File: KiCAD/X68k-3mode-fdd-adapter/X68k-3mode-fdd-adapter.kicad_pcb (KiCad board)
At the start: 4 copper layers, 57.1 x 70 mm, 49 parts, among them J1 Conn_02x17_Odd_Even, J2 Double Row 3A Copper Alloy 34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, J3 Conn_01x04, J4 PH-4A, J5 SDIO, J6 Conn_01x04, J7 Conn_01x03_Pin, P1 USB_C_Plug_USB2.0, Q1 2SC2712, SW1 SW_DIP_x02, SW2 SW_SPDT, U1 CH32V003F4U6, U4 74HC153, U5 74HC153, U6 ULN2003A

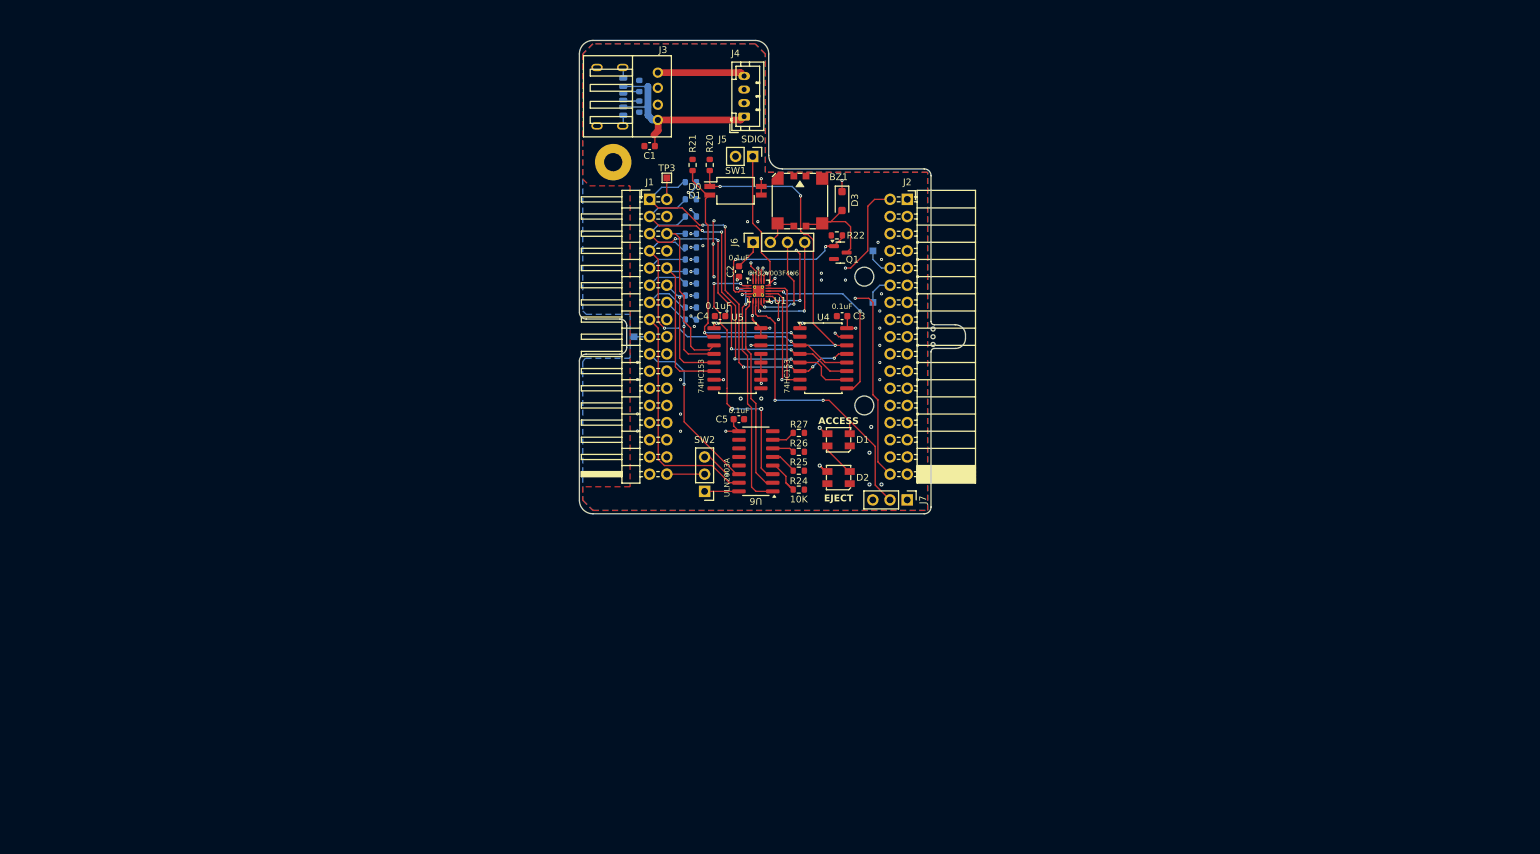
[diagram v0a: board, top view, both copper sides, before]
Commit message: フットプリントを一通り割り当てた
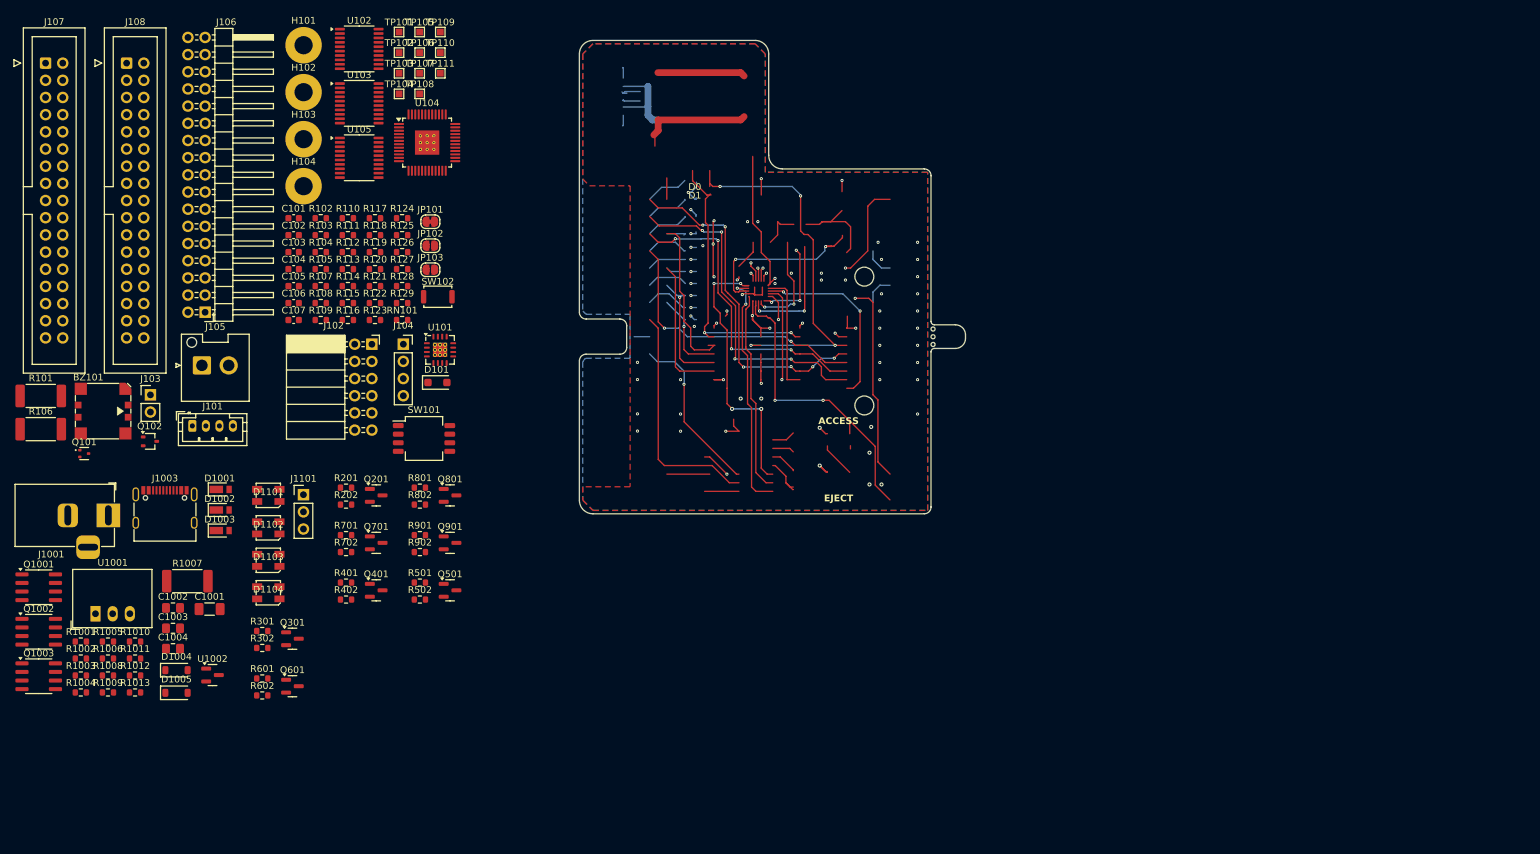
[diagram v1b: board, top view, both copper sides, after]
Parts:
- removed BZ1: Speaker, x68k-lib:UGCT7525AN4
- removed C1: 10uF, Capacitor_SMD:C_0603_1608Metric
- removed C2, C3, C4, C5: 0.1uF, Capacitor_SMD:C_0603_1608Metric
- removed D1, D2: SK6812MINI, x68k-lib:SK6812MINI-HS
- removed D3: SS2040FL, Diode_SMD:D_SOD-123F
- removed H1: MountingHole_Pad, MountingHole:MountingHole_2.7mm_M2.5_Pad
- removed J1: Conn_02x17_Odd_Even, x68k-lib:PinHeader_2x17_P2.54mm_Horizontal_Mirror
- removed J2: Double Row 3A Copper Alloy 34P Female Headers (PM254-2-17-W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, x68k-lib:PinSocket_2x17_P2.54mm_Horizontal_Mirror
- removed J3: Conn_01x04, x68k-lib:TE_AMP_171826-4
- removed J4: PH-4A, Connector_JST:JST_PH_B4B-PH-K_1x04_P2.00mm_Vertical
- removed J5: SDIO, Connector_PinHeader_2.54mm:PinHeader_1x02_P2.54mm_Vertical
- removed J6: Conn_01x04, Connector_PinSocket_2.54mm:PinSocket_1x04_P2.54mm_Vertical
- removed J7: Conn_01x03_Pin, Connector_PinHeader_2.54mm:PinHeader_1x03_P2.54mm_Vertical
- removed P1: USB_C_Plug_USB2.0, Connector_USB:USB_C_Receptacle_GCT_USB4125-xx-x-0190_6P_TopMnt_Horizontal
- removed Q1: 2SC2712, Package_TO_SOT_SMD:SOT-23
- removed R0, R1, R10, R11, R12, R13, R2, R3, R5, R6, R7: 1K, Resistor_SMD:R_0603_1608Metric
- removed R20, R21, R22, R24, R25, R26, R27: 10K, Resistor_SMD:R_0603_1608Metric
- removed R31, R32: 5.1k, Resistor_SMD:R_0603_1608Metric
- removed SW1: SW_DIP_x02, Button_Switch_SMD:SW_DIP_SPSTx02_Slide_Copal_CHS-02B_W7.62mm_P1.27mm
- removed SW2: SW_SPDT, Connector_PinHeader_2.54mm:PinHeader_1x03_P2.54mm_Vertical
- removed TP1, TP2, TP3, TP4: TestPoint, TestPoint:TestPoint_Pad_1.0x1.0mm
- removed U1: CH32V003F4U6, Package_DFN_QFN:QFN-20-1EP_3x3mm_P0.4mm_EP1.65x1.65mm_ThermalVias
- removed U4, U5: 74HC153, Package_SO:SO-16_5.3x10.2mm_P1.27mm
- removed U6: ULN2003A, Package_SO:SOP-16_3.9x9.9mm_P1.27mm
- added BZ101: Speaker, x68k-lib:UGCT7525AN4, F.Cu at (-8.43, 94.8)
- added C1001: 4.7uF 50V, Capacitor_SMD:C_1206_3216Metric_Pad1.33x1.80mm_HandSolder, F.Cu at (7.31, 124.1)
- added C1002: 22uF 25V, Capacitor_SMD:C_0805_2012Metric_Pad1.18x1.45mm_HandSolder, F.Cu at (1.90, 123.9)
- added C1003: 2.2uF 25V, Capacitor_SMD:C_0805_2012Metric_Pad1.18x1.45mm_HandSolder, F.Cu at (1.90, 126.9)
- added C1004: 2.2uF 25V, Capacitor_SMD:C_0805_2012Metric_Pad1.18x1.45mm_HandSolder, F.Cu at (1.90, 129.9)
- added C101: 0.1uF, Capacitor_SMD:C_0603_1608Metric, F.Cu at (19.7, 66.3)
- added C102: 0.1uF, Capacitor_SMD:C_0603_1608Metric, F.Cu at (19.7, 68.8)
- added C103: 0.1uF, Capacitor_SMD:C_0603_1608Metric, F.Cu at (19.7, 71.3)
- added C104: 0.1uF, Capacitor_SMD:C_0603_1608Metric, F.Cu at (19.7, 73.8)
- added C105: 0.1uF, Capacitor_SMD:C_0603_1608Metric, F.Cu at (19.7, 76.3)
- added C106: 0.1uF, Capacitor_SMD:C_0603_1608Metric, F.Cu at (19.7, 78.8)
- added C107: 0.1uF, Capacitor_SMD:C_0603_1608Metric, F.Cu at (19.7, 81.3)
- added D1001: CUHS20S30, x68k-lib:CUHS20S30 (US2H), F.Cu at (8.80, 106.4)
- added D1002: CUHS20S30, x68k-lib:CUHS20S30 (US2H), F.Cu at (8.80, 109.4)
- added D1003: CUHS20S30, x68k-lib:CUHS20S30 (US2H), F.Cu at (8.80, 112.5)
- added D1004: 1N60PW, Diode_SMD:D_SOD-123, F.Cu at (2.42, 133.1)
- added D1005: 1N60PW, Diode_SMD:D_SOD-123, F.Cu at (2.42, 136.5)
- added D101: SS2040FL, Diode_SMD:D_SOD-123F, F.Cu at (41.0, 90.6)
- added D1101: SK6812MINI, x68k-lib:SK6812MINI-HS, F.Cu at (16.0, 107.3)
- added D1102: SK6812MINI, x68k-lib:SK6812MINI-HS, F.Cu at (16.0, 112.1)
- added D1103: SK6812MINI, x68k-lib:SK6812MINI-HS, F.Cu at (16.0, 116.9)
- added D1104: SK6812MINI, x68k-lib:SK6812MINI-HS, F.Cu at (16.0, 121.7)
- added H101: MountingHole_Pad, MountingHole:MountingHole_2.7mm_M2.5_Pad, F.Cu at (21.2, 40.7)
- added H102: MountingHole_Pad, MountingHole:MountingHole_2.7mm_M2.5_Pad, F.Cu at (21.2, 47.7)
- added H103: MountingHole_Pad, MountingHole:MountingHole_2.7mm_M2.5_Pad, F.Cu at (21.2, 54.6)
- added H104: MountingHole_Pad, MountingHole:MountingHole_2.7mm_M2.5_Pad, F.Cu at (21.2, 61.6)
- added J1001: Barrel_Jack_Switch, Connector_BarrelJack:BarrelJack_Horizontal, F.Cu at (-7.66, 110.2)
- added J1003: USB_C_Receptacle_USB2.0_16P, Connector_USB:USB_C_Receptacle_G-Switch_GT-USB-7010ASV, F.Cu at (0.71, 110.3)
- added J101: 4pin, Connector_JST:JST_PH_B4B-PH-K_1x04_P2.00mm_Vertical, F.Cu at (4.76, 97.0)
- added J102: Conn_02x06_Odd_Even, Connector_PinSocket_2.54mm:PinSocket_2x06_P2.54mm_Horizontal, F.Cu at (31.3, 84.9)
- added J103: Conn_01x02, Connector_PinHeader_2.54mm:PinHeader_1x02_P2.54mm_Vertical, F.Cu at (-1.44, 92.4)
- added J104: Conn_01x04, Connector_PinSocket_2.54mm:PinSocket_1x04_P2.54mm_Vertical, F.Cu at (36.0, 84.9)
- added J105: Conn_01x02, Connector_JST:JST_VH_B2P-VH-FB-B_1x02_P3.96mm_Vertical, F.Cu at (6.18, 88.1)
- added J106: Conn_02x17_Odd_Even, x68k-lib:PinHeader_2x17_P2.54mm_Horizontal_Mirror, F.Cu at (4.11, 39.6)
- added J107: Conn_02x17_Odd_Even, Connector_IDC:IDC-Header_2x17_P2.54mm_Vertical, F.Cu at (-16.9, 43.4)
- added J108: Conn_02x17_Odd_Even, Connector_IDC:IDC-Header_2x17_P2.54mm_Vertical, F.Cu at (-4.96, 43.4)
- added J1101: Conn_01x03_Pin, Connector_PinHeader_2.54mm:PinHeader_1x03_P2.54mm_Vertical, F.Cu at (21.2, 107.2)
- added JP101: Jumper_2_Small_Bridged, Jumper:SolderJumper-2_P1.3mm_Bridged_RoundedPad1.0x1.5mm, F.Cu at (40.0, 66.8)
- added JP102: Jumper_2_Small_Open, Jumper:SolderJumper-2_P1.3mm_Open_RoundedPad1.0x1.5mm, F.Cu at (40.0, 70.4)
- added JP103: Jumper_2_Small_Open, Jumper:SolderJumper-2_P1.3mm_Open_RoundedPad1.0x1.5mm, F.Cu at (40.0, 73.9)
- added Q1001: FDS4935A, Package_SO:SOIC-8_3.9x4.9mm_P1.27mm, F.Cu at (-18.0, 120.9)
- added Q1002: FDS4935A, Package_SO:SOIC-8_3.9x4.9mm_P1.27mm, F.Cu at (-18.0, 127.4)
- added Q1003: FDS4935A, Package_SO:SOIC-8_3.9x4.9mm_P1.27mm, F.Cu at (-18.0, 134.0)
- added Q101: DTC143Z, Package_TO_SOT_SMD:SOT-523, F.Cu at (-11.2, 101.1)
- added Q102: 2SC2712, Package_TO_SOT_SMD:SOT-323_SC-70, F.Cu at (-1.51, 99.3)
- added Q201: BSS138, Package_TO_SOT_SMD:SOT-23, F.Cu at (32.0, 107.3)
- added Q301: BSS138, Package_TO_SOT_SMD:SOT-23, F.Cu at (19.6, 128.5)
- added Q401: BSS138, Package_TO_SOT_SMD:SOT-23, F.Cu at (32.0, 121.3)
- added Q501: BSS138, Package_TO_SOT_SMD:SOT-23, F.Cu at (42.9, 121.3)
- added Q601: BSS138, Package_TO_SOT_SMD:SOT-23, F.Cu at (19.6, 135.5)
- added Q701: BSS138, Package_TO_SOT_SMD:SOT-23, F.Cu at (32.0, 114.3)
- added Q801: BSS138, Package_TO_SOT_SMD:SOT-23, F.Cu at (42.9, 107.3)
- added Q901: BSS138, Package_TO_SOT_SMD:SOT-23, F.Cu at (42.9, 114.3)
- added R1001: 100k, Resistor_SMD:R_0603_1608Metric, F.Cu at (-11.7, 128.9)
- added R1002: 10k, Resistor_SMD:R_0603_1608Metric, F.Cu at (-11.7, 131.4)
- added R1003: 100k, Resistor_SMD:R_0603_1608Metric, F.Cu at (-11.7, 133.9)
- added R1004: 10k, Resistor_SMD:R_0603_1608Metric, F.Cu at (-11.7, 136.4)
- added R1005: 100k, Resistor_SMD:R_0603_1608Metric, F.Cu at (-7.72, 128.9)
- added R1006: 10k, Resistor_SMD:R_0603_1608Metric, F.Cu at (-7.72, 131.4)
- added R1007: R100 (0.1Ω), Resistor_SMD:R_2512_6332Metric_Pad1.40x3.35mm_HandSolder, F.Cu at (4.02, 120.0)
- added R1008: 220, Resistor_SMD:R_0603_1608Metric, F.Cu at (-7.72, 133.9)
- added R1009: 1k, Resistor_SMD:R_0603_1608Metric, F.Cu at (-7.72, 136.4)
- added R101: R100 (0.1Ω), Resistor_SMD:R_2512_6332Metric_Pad1.40x3.35mm_HandSolder, F.Cu at (-17.7, 92.6)
- added R1010: 220, Resistor_SMD:R_0603_1608Metric, F.Cu at (-3.71, 128.9)
- added R1011: 1k, Resistor_SMD:R_0603_1608Metric, F.Cu at (-3.71, 131.4)
- added R1012: 5.1k, Resistor_SMD:R_0603_1608Metric, F.Cu at (-3.71, 133.9)
- added R1013: 5.1k, Resistor_SMD:R_0603_1608Metric, F.Cu at (-3.71, 136.4)
- added R102: 10K, Resistor_SMD:R_0603_1608Metric, F.Cu at (23.8, 66.3)
- added R103: 10K, Resistor_SMD:R_0603_1608Metric, F.Cu at (23.8, 68.8)
- added R104: 10K, Resistor_SMD:R_0603_1608Metric, F.Cu at (23.8, 71.3)
- added R105: 10K, Resistor_SMD:R_0603_1608Metric, F.Cu at (23.8, 73.8)
- added R106: R100 (0.1Ω), Resistor_SMD:R_2512_6332Metric_Pad1.40x3.35mm_HandSolder, F.Cu at (-17.7, 97.5)
- added R107: 10K, Resistor_SMD:R_0603_1608Metric, F.Cu at (23.8, 76.3)
- added R108: 1K, Resistor_SMD:R_0603_1608Metric, F.Cu at (23.8, 78.8)
- added R109: 1K, Resistor_SMD:R_0603_1608Metric, F.Cu at (23.8, 81.3)
- added R110: 1K, Resistor_SMD:R_0603_1608Metric, F.Cu at (27.8, 66.3)
- added R111: 1K, Resistor_SMD:R_0603_1608Metric, F.Cu at (27.8, 68.8)
- added R112: 1K, Resistor_SMD:R_0603_1608Metric, F.Cu at (27.8, 71.3)
- added R113: 1K, Resistor_SMD:R_0603_1608Metric, F.Cu at (27.8, 73.8)
- added R114: 1K, Resistor_SMD:R_0603_1608Metric, F.Cu at (27.8, 76.3)
- added R115: 1K, Resistor_SMD:R_0603_1608Metric, F.Cu at (27.8, 78.8)
- added R116: 1K, Resistor_SMD:R_0603_1608Metric, F.Cu at (27.8, 81.3)
- added R117: 2.2k, Resistor_SMD:R_0603_1608Metric, F.Cu at (31.8, 66.3)
- added R118: 2.2k, Resistor_SMD:R_0603_1608Metric, F.Cu at (31.8, 68.8)
- added R119: 1K, Resistor_SMD:R_0603_1608Metric, F.Cu at (31.8, 71.3)
- added R120: 1K, Resistor_SMD:R_0603_1608Metric, F.Cu at (31.8, 73.8)
- added R121: 1K, Resistor_SMD:R_0603_1608Metric, F.Cu at (31.8, 76.3)
- added R122: 1K, Resistor_SMD:R_0603_1608Metric, F.Cu at (31.8, 78.8)
- added R123: 1K, Resistor_SMD:R_0603_1608Metric, F.Cu at (31.8, 81.3)
- added R124: 1K, Resistor_SMD:R_0603_1608Metric, F.Cu at (35.8, 66.3)
- added R125: 1K, Resistor_SMD:R_0603_1608Metric, F.Cu at (35.8, 68.8)
- added R126: 1K, Resistor_SMD:R_0603_1608Metric, F.Cu at (35.8, 71.3)
- added R127: 1K, Resistor_SMD:R_0603_1608Metric, F.Cu at (35.8, 73.8)
- added R128: 1K, Resistor_SMD:R_0603_1608Metric, F.Cu at (35.8, 76.3)
- added R129: 1k, Resistor_SMD:R_0603_1608Metric, F.Cu at (35.8, 78.8)
- added R201: 100, Resistor_SMD:R_0603_1608Metric, F.Cu at (27.5, 106.1)
- added R202: 100, Resistor_SMD:R_0603_1608Metric, F.Cu at (27.5, 108.6)
- added R301: 100, Resistor_SMD:R_0603_1608Metric, F.Cu at (15.1, 127.3)
- added R302: 100, Resistor_SMD:R_0603_1608Metric, F.Cu at (15.1, 129.8)
- added R401: 100, Resistor_SMD:R_0603_1608Metric, F.Cu at (27.5, 120.2)
- added R402: 100, Resistor_SMD:R_0603_1608Metric, F.Cu at (27.5, 122.7)
- added R501: 100, Resistor_SMD:R_0603_1608Metric, F.Cu at (38.4, 120.2)
- added R502: 100, Resistor_SMD:R_0603_1608Metric, F.Cu at (38.4, 122.7)
- added R601: 100, Resistor_SMD:R_0603_1608Metric, F.Cu at (15.1, 134.4)
- added R602: 100, Resistor_SMD:R_0603_1608Metric, F.Cu at (15.1, 136.9)
- added R701: 100, Resistor_SMD:R_0603_1608Metric, F.Cu at (27.5, 113.2)
- added R702: 100, Resistor_SMD:R_0603_1608Metric, F.Cu at (27.5, 115.7)
- added R801: 100, Resistor_SMD:R_0603_1608Metric, F.Cu at (38.4, 106.1)
- added R802: 100, Resistor_SMD:R_0603_1608Metric, F.Cu at (38.4, 108.6)
- added R901: 100, Resistor_SMD:R_0603_1608Metric, F.Cu at (38.4, 113.2)
- added R902: 100, Resistor_SMD:R_0603_1608Metric, F.Cu at (38.4, 115.7)
- added RN101: 4.7k, Resistor_SMD:R_0603_1608Metric, F.Cu at (35.8, 81.3)
- added SW101: SW_DIP_x04, Button_Switch_SMD:SW_DIP_SPSTx04_Slide_Copal_CHS-04B_W7.62mm_P1.27mm, F.Cu at (39.0, 98.9)
- added SW102: RESET_SW, Button_Switch_SMD:SW_Push_SPST_NO_Alps_SKRK, F.Cu at (41.1, 77.9)
- added TP101: TestPoint, TestPoint:TestPoint_Pad_1.0x1.0mm, F.Cu at (35.3, 38.8)
- added TP102: TestPoint, TestPoint:TestPoint_Pad_1.0x1.0mm, F.Cu at (35.3, 41.8)
- added TP103: TestPoint, TestPoint:TestPoint_Pad_1.0x1.0mm, F.Cu at (35.3, 44.9)
- added TP104: TestPoint, TestPoint:TestPoint_Pad_1.0x1.0mm, F.Cu at (35.3, 47.9)
- added TP105: TestPoint, TestPoint:TestPoint_Pad_1.0x1.0mm, F.Cu at (38.4, 38.8)
- added TP106: TestPoint, TestPoint:TestPoint_Pad_1.0x1.0mm, F.Cu at (38.4, 41.8)
- added TP107: TestPoint, TestPoint:TestPoint_Pad_1.0x1.0mm, F.Cu at (38.4, 44.9)
- added TP108: TestPoint, TestPoint:TestPoint_Pad_1.0x1.0mm, F.Cu at (38.4, 47.9)
- added TP109: TestPoint, TestPoint:TestPoint_Pad_1.0x1.0mm, F.Cu at (41.4, 38.8)
- added TP110: TestPoint, TestPoint:TestPoint_Pad_1.0x1.0mm, F.Cu at (41.4, 41.8)
- added TP111: TestPoint, TestPoint:TestPoint_Pad_1.0x1.0mm, F.Cu at (41.4, 44.9)
- added U1001: K7805M-1000R3, Converter_DCDC:Converter_DCDC_RECOM_R-78E-0.5_THT, F.Cu at (-9.56, 124.8)
- added U1002: MCP1792x-5002xCB, Package_TO_SOT_SMD:SOT-23, F.Cu at (7.74, 133.8)
- added U101: INA3221AIRGVR, Package_DFN_QFN:QFN-16-1EP_4x4mm_P0.65mm_EP2.1x2.1mm_ThermalVias, F.Cu at (41.4, 85.8)
- added U102: SLG46826G(V2), Package_SO:TSSOP-20_4.4x6.5mm_P0.65mm, F.Cu at (29.4, 41.3)
- added U103: SLG46826G(V2), Package_SO:TSSOP-20_4.4x6.5mm_P0.65mm, F.Cu at (29.4, 49.3)
- added U104: CH32X035C8T6, Package_QFP:LQFP-48-1EP_7x7mm_P0.5mm_EP3.6x3.6mm_ThermalVias, F.Cu at (39.5, 55.1)
- added U105: SLG46826G(V2), Package_SO:TSSOP-20_4.4x6.5mm_P0.65mm, F.Cu at (29.4, 57.4)
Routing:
- net (no net): track 0.00 -> 508.6 mm, vias 0 -> 42
- net +5V: track 80.8 -> 0.00 mm, vias 20 -> 0
- net /DIPSW_0: track 56.7 -> 0.00 mm, vias 4 -> 0
- net /DIPSW_1: track 42.2 -> 0.00 mm, vias 2 -> 0
- net /FDD_INT_GEN: track 40.8 -> 0.00 mm, vias 4 -> 0
- net /READY_GEN: track 36.2 -> 0.00 mm, vias 2 -> 0
- net /DISK_IN_GEN: track 30.0 -> 0.00 mm
- net /OPTION_SELECT_PAIR: track 27.6 -> 0.00 mm, vias 2 -> 0
- net /DRIVE_SELECT_DOSV_1: track 27.2 -> 0.00 mm, vias 1 -> 0
- net /DRIVE_SELECT: track 25.5 -> 0.00 mm, vias 2 -> 0
- net /FDD_INT_BUF: track 25.0 -> 0.00 mm, vias 1 -> 0
- net /OPTION_SELECT: track 18.0 -> 0.00 mm
- net /SDA: track 17.7 -> 0.00 mm, vias 2 -> 0
- net /SCL: track 15.2 -> 0.00 mm, vias 2 -> 0
- net Net-(D3-A): track 14.7 -> 0.00 mm
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- added copper zone on In1.Cu, net (none)
- removed copper zone on In1.Cu, net +5V

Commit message: PCBの配線完了
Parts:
- removed J1101: Conn_01x03_Pin, Connector_PinHeader_2.54mm:PinHeader_1x03_P2.54mm_Vertical
- removed R1009, R1011: 1k, Resistor_SMD:R_0603_1608Metric
- removed R123: 1K, Resistor_SMD:R_0603_1608Metric
- added H105: MountingHole_Pad, x68k-lib:PCB_WeldingTerminal_M3_L-angle_PCB-54L, F.Cu at (197.0, 57.0)
- added H106: MountingHole_Pad, x68k-lib:PCB_WeldingTerminal_M3_L-angle_PCB-54R, F.Cu at (197.0, 137.0)
- C1001, C1002, C101, C102, C103, C104, C106, C107, D1002, JP101, R1008, R101, R1010, R1012, R1013, R106, R113, R114, R115, R116, R124, R125, R126, TP103, TP104, TP106, U101: moved to B.Cu
- H101, H102, H103, H104: footprint MountingHole:MountingHole_2.7mm_M2.5_Pad -> x68k-lib:PCB_WeldingTerminal_M3_L-angle; moved to B.Cu
- J101: footprint Connector_JST:JST_PH_B4B-PH-K_1x04_P2.00mm_Vertical -> TerminalBlock_Phoenix:TerminalBlock_Phoenix_MPT-0,5-4-2.54_1x04_P2.54mm_Horizontal
- J107, J108: footprint Connector_IDC:IDC-Header_2x17_P2.54mm_Vertical -> Connector_PinHeader_2.54mm:PinHeader_2x17_P2.54mm_Horizontal; moved to B.Cu
- RN101: value 4.7k -> 4.7k x4; footprint Resistor_SMD:R_0603_1608Metric -> Resistor_SMD:R_Array_Concave_4x0603; moved to B.Cu
- moved J108 205.6 mm to (195.6, 88.9), turned to 180 degrees
- moved BZ101 191.0 mm to (177.8, 137.2)
- moved H104 190.6 mm to (194.0, 142.0), turned to -90 degrees
- moved J107 186.4 mm to (163.8, 88.9), turned to 180 degrees
- moved Q102 176.5 mm to (170.5, 139.0)
- moved H103 172.8 mm to (194.0, 52.0), turned to 90 degrees
- moved D1101 167.8 mm to (183.8, 111.7)
- moved D1102 167.8 mm to (183.8, 116.5)
- moved D1103 167.8 mm to (183.8, 121.3)
- moved D1104 167.8 mm to (183.8, 126.1)
- moved TP108 160.5 mm to (190.5, 99.1)
- moved R107 156.8 mm to (167.5, 139.0), turned to -90 degrees
- moved J102 155.7 mm to (187.0, 81.0), turned to 180 degrees
- moved R502 148.5 mm to (185.4, 101.6), turned to 90 degrees
- moved Q501 147.1 mm to (188.6, 101.6)
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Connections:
- J101 pad 1: +5V_FDD -> +12V_FDD
- J101 pad 4: +12V_FDD -> +5V_FDD
- R1008 pad 2: Net-(R1008-Pad2) -> /CC1
- R1010 pad 2: Net-(R1010-Pad2) -> /CC2
- R1012 pad 1: Net-(R1010-Pad2) -> /CC2
- R1013 pad 1: Net-(R1008-Pad2) -> /CC1
- R105 pad 1: /DIPSW_MODESEL_POL -> /DIPSW_12V_REQ
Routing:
- net (no net): track 508.6 -> 0.00 mm, vias 42 -> 0
- net VDD_MCU: track 0.00 -> 195.0 mm, vias 0 -> 17
- net /I2C_SCL: track 0.00 -> 189.2 mm, vias 0 -> 10
- net /I2C_SDA: track 0.00 -> 176.6 mm, vias 0 -> 10
- net VDD_FDDIF: track 0.00 -> 131.7 mm, vias 0 -> 24
- net /INDEX_DOSV: track 0.00 -> 110.7 mm, vias 0 -> 5
- net /USB_D-: track 0.00 -> 106.0 mm, vias 0 -> 7
- net GND: track 133.5 -> 27.6 mm, vias 48 -> 11
- net /USB_D+: track 0.00 -> 103.9 mm, vias 0 -> 6
- net /READ_DATA_DOSV: track 0.00 -> 103.4 mm, vias 0 -> 4
- net /TRACK_00_DOSV: track 0.00 -> 99.1 mm, vias 0 -> 3
- net /WRITE_DATA_DOSV: track 0.00 -> 92.3 mm, vias 0 -> 3
- net /WRITE_PROTECT_DOSV: track 0.00 -> 88.5 mm, vias 0 -> 2
- net /+12V_EXT_DET: track 0.00 -> 88.1 mm, vias 0 -> 4
- net /WRITE_GATE_DOSV: track 0.00 -> 87.2 mm, vias 0 -> 2
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- added copper zone on In1.Cu, net VDD_FDDIF
- added copper zone on In1.Cu, net VDD_MCU
- removed copper zone on In1.Cu, net (none)
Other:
- board size 57.1 x 70 mm -> 129 x 94 mm
- board text added: "FDD A"
- board text added: "FDD B"
- board text added: "RED LINE"
- board text removed: "ACCESS"
- board text removed: "D0"
- board text removed: "D1"
- board text removed: "DSEL0"
- board text removed: "DSEL1"
- board text removed: "EDSK"
- board text removed: "EJECT"

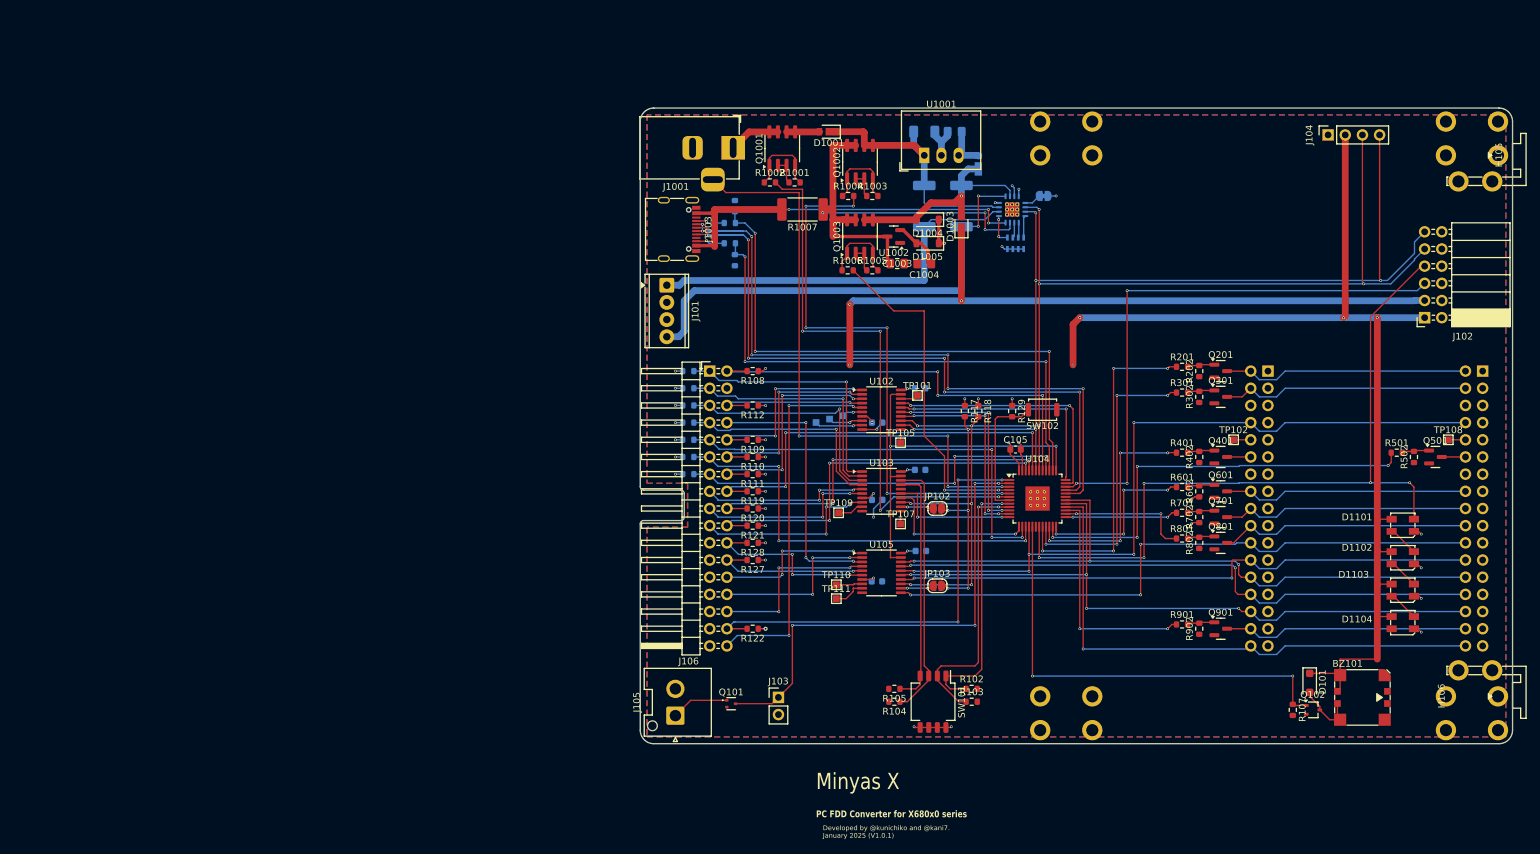
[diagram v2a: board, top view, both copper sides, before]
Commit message: 基板の外径を変更して、底面部のネジ穴に合うホールを追加
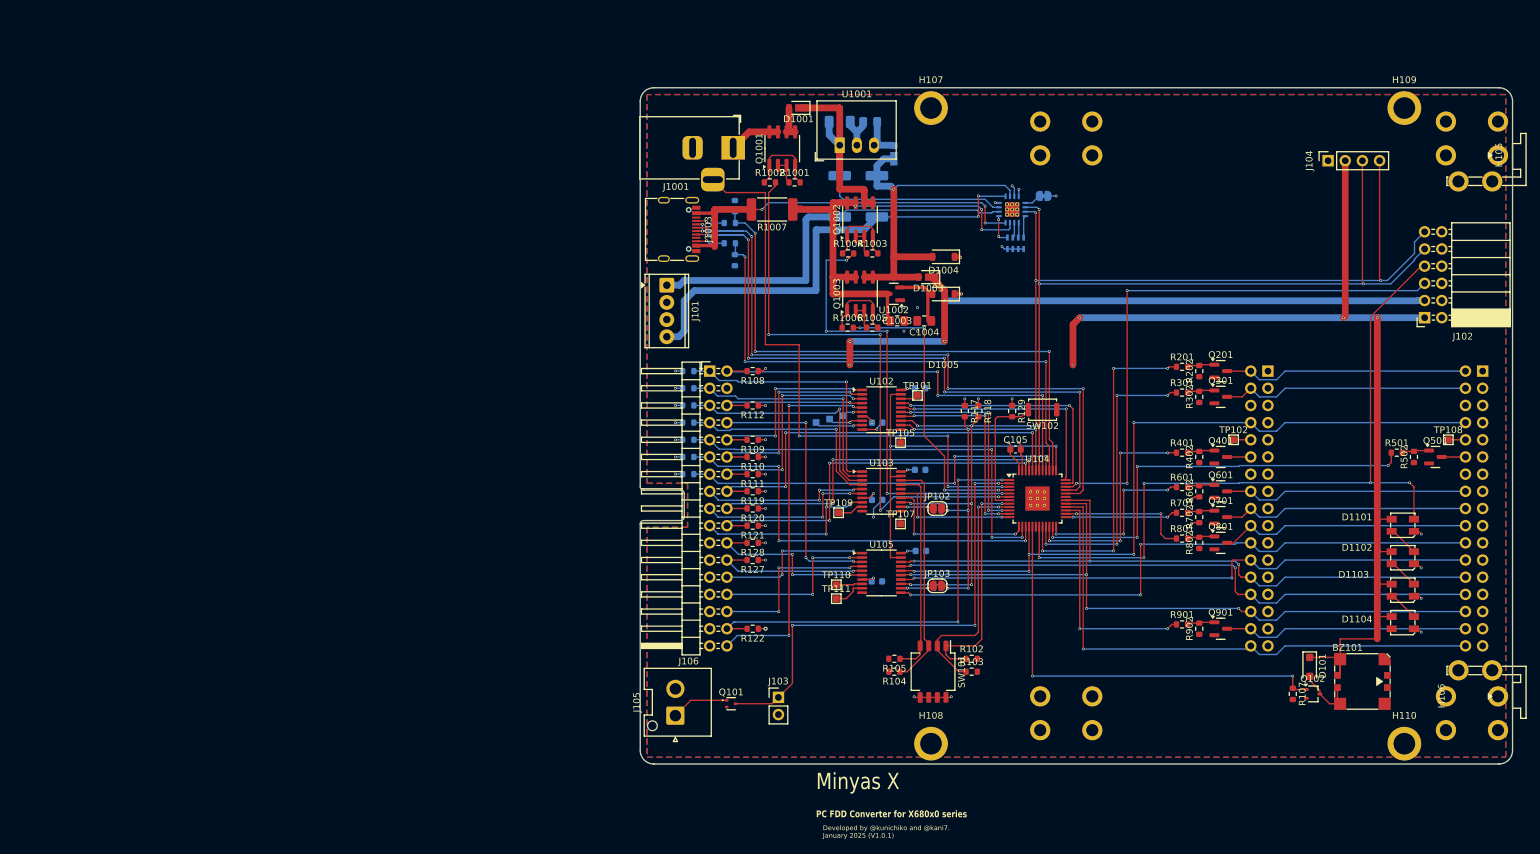
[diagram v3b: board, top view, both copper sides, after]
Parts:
- added H107: MountingHole_Pad, x68k-lib:MountingHole_3.2mm_M3_Pad_Small, F.Cu at (114.0, 50.0)
- added H108: MountingHole_Pad, x68k-lib:MountingHole_3.2mm_M3_Pad_Small, F.Cu at (114.0, 144.0)
- added H109: MountingHole_Pad, x68k-lib:MountingHole_3.2mm_M3_Pad_Small, F.Cu at (184.0, 50.0)
- added H110: MountingHole_Pad, x68k-lib:MountingHole_3.2mm_M3_Pad_Small, F.Cu at (184.0, 144.0)
- moved D1002 12.6 mm to (108.5, 57.0)
- moved U1001 12.6 mm to (100.5, 55.5)
- moved C1001 12.6 mm to (100.5, 52.0)
- moved C1002 12.6 mm to (105.0, 52.0)
- moved R101 12.6 mm to (100.5, 63.0)
- moved R106 12.6 mm to (106.0, 63.0)
- moved D1003 8.96 mm to (113.6, 75.0), turned to 180 degrees
- moved Q1002 8.50 mm to (103.5, 66.5)
- moved R1003 8.50 mm to (105.3, 71.5)
- moved R1004 8.50 mm to (101.7, 71.5)
- moved C1003 8.47 mm to (109.0, 81.5)
- moved C1004 8.47 mm to (113.0, 81.5)
- moved Q1003 8.47 mm to (103.5, 77.5)
- moved R1005 8.47 mm to (105.3, 82.5)
- moved R1006 8.47 mm to (101.7, 82.5)
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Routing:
- net /+12V_FDD_S: track 38.6 -> 60.3 mm
- net /+5V_FDD_S: track 33.4 -> 53.9 mm
- net /+12V_ENABLE_n: track 81.1 -> 66.1 mm, vias 6 -> 5
- net VDD_MCU: track 195.0 -> 182.3 mm, vias 17 -> 18
- net VDD_FDDIF: track 131.7 -> 125.7 mm, vias 24 -> 25
- net /+5V_ENABLE_n: track 50.3 -> 45.3 mm, vias 2 -> 4
- net /DIPSW_DS1: track 41.6 -> 37.2 mm
- net /DIPSW_DS0: track 38.8 -> 34.4 mm
- net /DIPSW_12V_REQ: track 35.6 -> 31.2 mm
- net /I2C_SDA: track 176.6 -> 172.8 mm
- net /I2C_SCL: track 189.2 -> 185.4 mm
- net /DIPSW_MODESEL_POL: track 38.7 -> 35.0 mm
- net /BUZZER: track 66.8 -> 64.5 mm
- net Net-(D1005-A): track 7.30 -> 9.41 mm
- net /+12V_EXT_ENABLE_n: track 83.3 -> 85.3 mm
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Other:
- board size 129 x 94 mm -> 129 x 100 mm
